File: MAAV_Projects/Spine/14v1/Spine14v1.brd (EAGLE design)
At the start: 124.5 x 101.6 mm, 91 parts, among them J7 MA04-1, Q1 MOSFET-NCHANNELSMD, Q2 MOSFET-NCHANNELSMD, Q21 P-MOSFET-SO8POWER-PAK, Q22 P-MOSFET-SO8POWER-PAK, Q23 P-MOSFET-SO8POWER-PAK, Q24 P-MOSFET-SO8POWER-PAK, Q3 MOSFET-NCHANNELSMD, Q4 MOSFET-NCHANNELSMD, Q5 P-MOSFET-SO8POWER-PAK, Q6 MOSFET-NCHANNELSMD, Q7 MOSFET-NCHANNELSMD, Q8 MOSFET-NCHANNELSMD, U1 ATMEGA328-AU, U3 XC6210

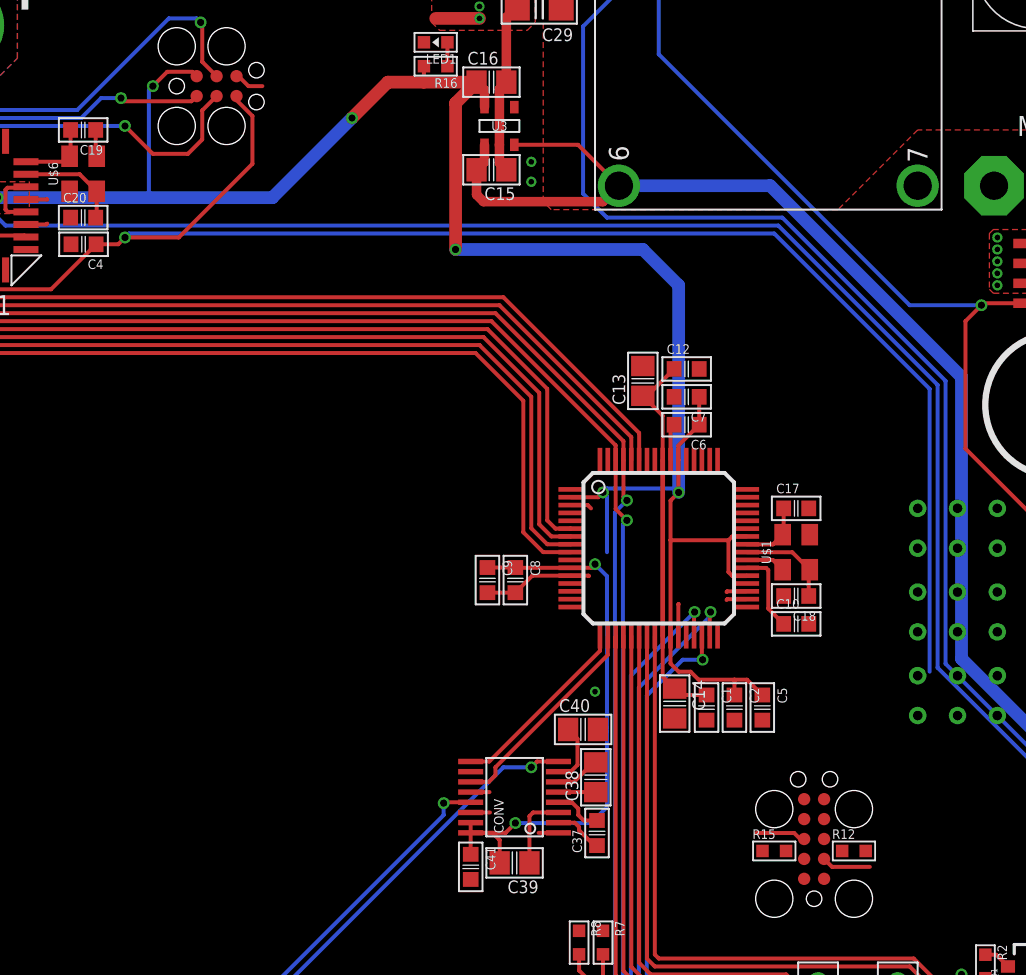
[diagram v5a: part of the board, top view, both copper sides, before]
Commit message: finished JTAG routing. still need to finish the toggle switches
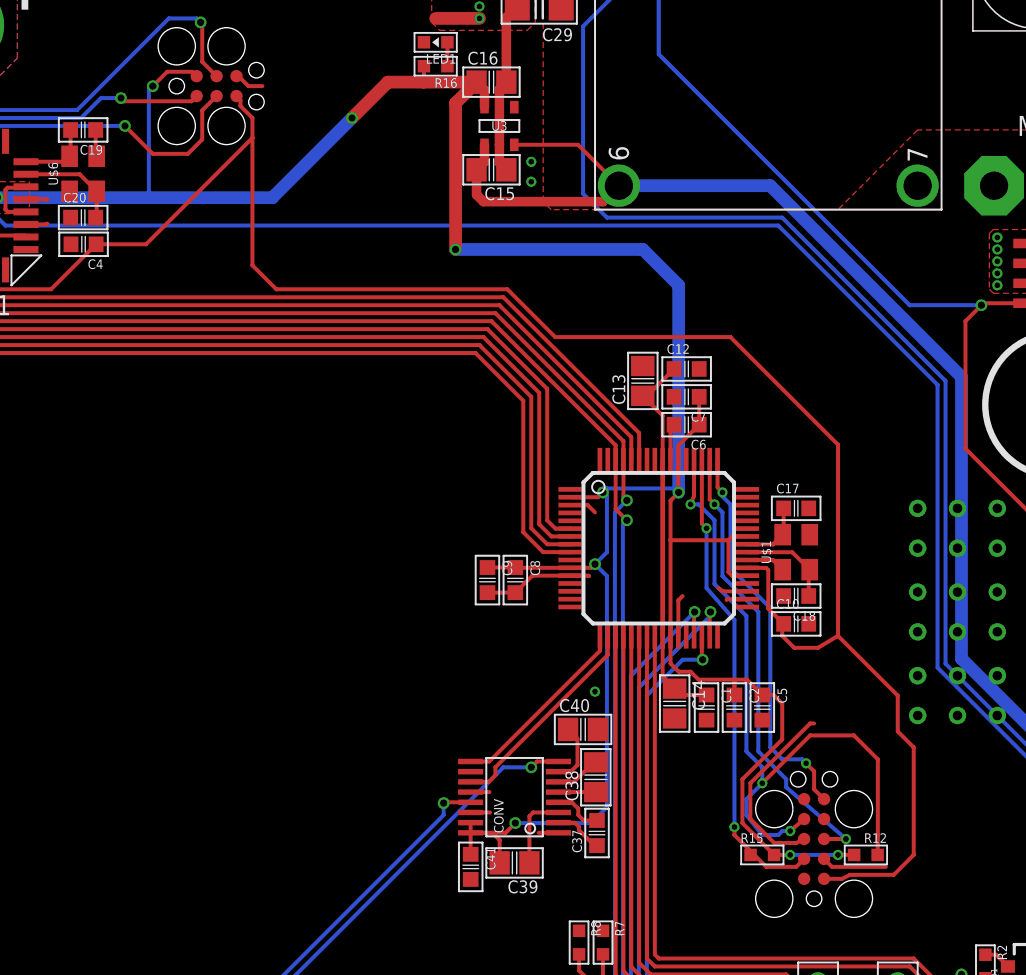
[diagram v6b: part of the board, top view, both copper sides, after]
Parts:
- moved R12 0.80 mm to (84.3, 22.1), turned to 180 degrees
- moved R15 0.80 mm to (77.7, 22.1)
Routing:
- net ICDI_TCK: track 0.00 -> 45.3 mm, vias 0 -> 3
- net ICDI_TMS: track 0.00 -> 30.3 mm, vias 0 -> 2
- net ICDI_TDI: track 0.00 -> 29.3 mm, vias 0 -> 2
- net ICDI_TDO: track 0.00 -> 25.2 mm, vias 0 -> 2
- net +3V3: track 198.7 -> 218.0 mm, vias 10 -> 12
- net RESET: track 143.9 -> 158.9 mm, vias 1 -> 0
- net GND: track 51.1 -> 62.5 mm

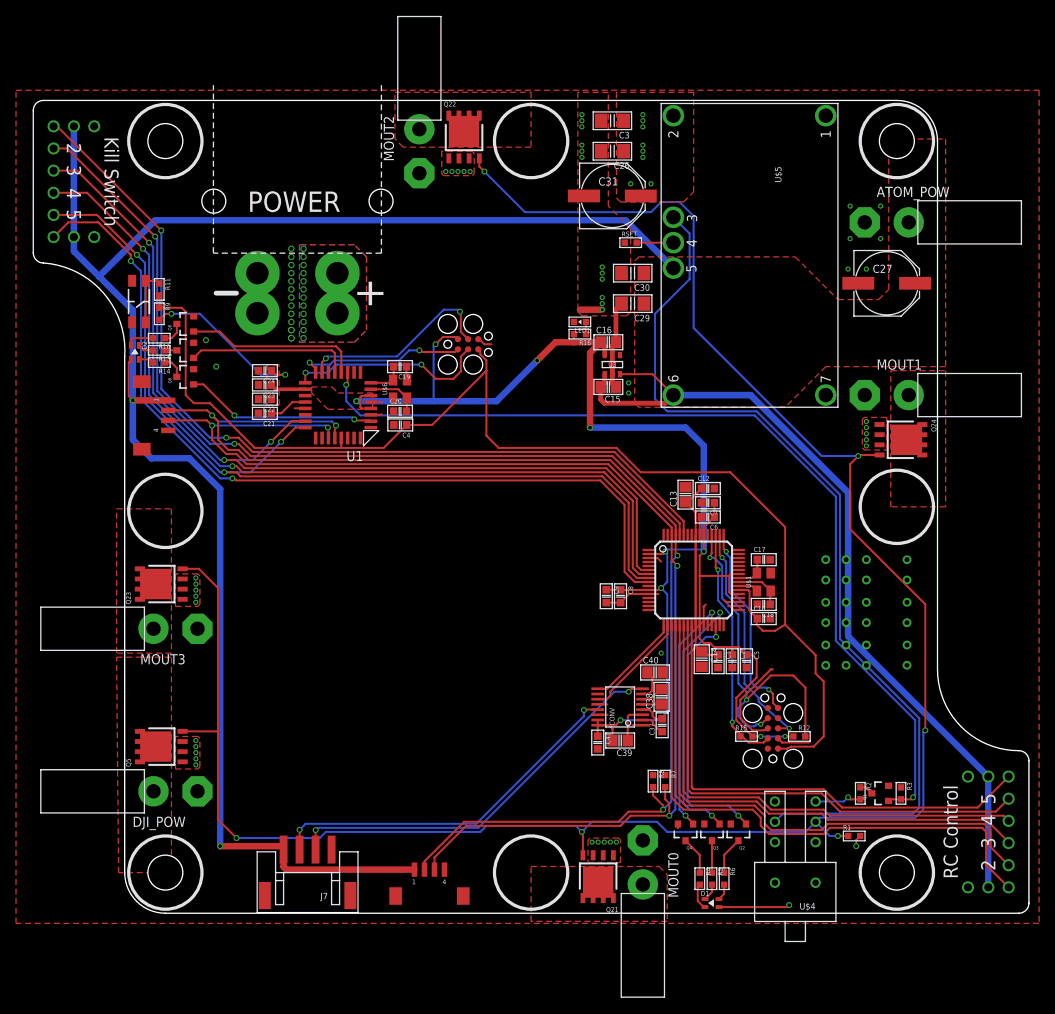
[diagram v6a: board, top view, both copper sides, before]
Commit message: put in toggle switches and finished routing the baord.  Added logo and credits
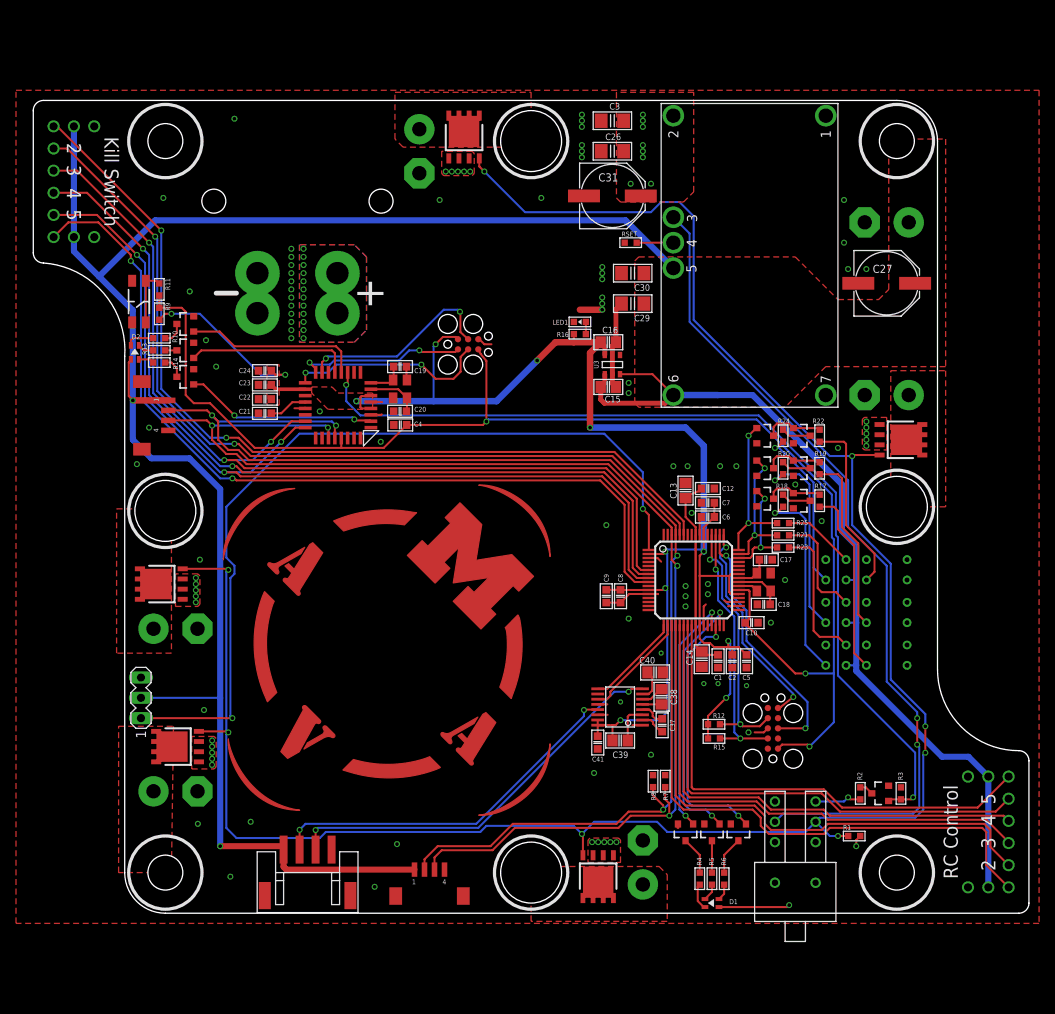
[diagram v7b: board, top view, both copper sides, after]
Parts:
- removed S4: SWITCH_SPDT_ILUMINATED_2COLOR_VERT_ILLUMINATED, Jon_LIB:NKK_VERT_SWITCH_6PIN
- added DJI_SIG: (no value), Jon_LIB:MA03-1
- added Q10, Q11, Q12, Q13, Q14, Q9: MOSFET-NCHANNELSMD, Jon_LIB:SOT23-3
- added R17, R18, R19, R20, R22, R24: 100, Jon_LIB:R0603
- added R21, R23, R25: 1k, Jon_LIB:R0603
- added S_R: (no value), Jon_LIB:TACT-MOM-SMD
- added U$8: (no value), maav-logos:MAAVLOGO_50MM_MASK_ONLY
- S1: value SWITCH_DPDT_VERT_TOGGLE -> SWITCH_SPDT_ILUMINATED_2COLOR_VERT_ILLUMINATED
- S2: value (none) -> SWITCH_SPDT_ILUMINATED_2COLOR_VERT_ILLUMINATED; device Jon_LIB:TACT-MOM-SMD -> Jon_LIB:NKK_VERT_SWITCH_6PIN
- moved S2 98.9 mm to (92.7, 37.6), turned to 90 degrees
- moved R12 10.8 mm to (73.7, 23.6)
- moved S1 10.7 mm to (92.7, 32.3)
- moved S3 5.33 mm to (92.7, 42.9)
- moved R15 4.07 mm to (73.7, 21.8), turned to 180 degrees
- moved Q5 2.03 mm to (6.60, 20.8)
- moved C10 1.61 mm to (78.4, 36.3)
- moved C13 0.51 mm to (70.1, 52.8)
- moved C17 0.25 mm to (80.1, 44.2)
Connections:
- new net DJI_PPM: DJI_SIG.1, U$3.P$1
- new net N$26: Q9.3, R18.1
- new net N$27: Q11.1, Q12.3, R19.1
- new net N$28: Q11.3, R20.1
- new net N$29: R19.2, S2.P$6
- new net N$30: R20.2, S2.P$4
- new net N$31: R23.2, S1.P$2
- new net N$33: R21.2, S2.P$2
- new net N$34: R17.2, S1.P$6
- new net N$37: R18.2, S1.P$4
- new net N$39: Q13.1, Q14.3, R22.1
- new net N$40: Q13.3, R24.1
- new net N$41: R22.2, S3.P$6
- new net N$42: R24.2, S3.P$4
- new net N$43: R25.2, S3.P$2
- new net N$9: Q10.3, Q9.1, R17.1
- new net OPT_SWITCH_1: Q10.1, R23.1, U$3.P$46
- new net OPT_SWITCH_2: Q12.1, R21.1, U$3.P$47
- new net OPT_SWITCH_3: Q14.1, R25.1, U$3.P$48
- net +5V: now also DJI_SIG.2, S1.P$5, S2.P$5, S3.P$5
- net GND: now also DJI_SIG.3, Q10.2, Q11.2, Q12.2, Q13.2, Q14.2, Q9.2, S1.P$1, S2.P$1, S3.P$1, S_R.S, S_R.S1; no longer S2.S, S2.S1
- net N$10: now also S_R.P, S_R.P1; no longer S2.P, S2.P1
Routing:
- net DJI_PPM: track 0.00 -> 106.5 mm, vias 0 -> 2
- net N$37: track 0.00 -> 24.8 mm, vias 0 -> 1
- net N$30: track 0.00 -> 24.6 mm, vias 0 -> 1
- net N$34: track 0.00 -> 23.3 mm
- net N$41: track 0.00 -> 22.3 mm
- net N$29: track 0.00 -> 22.3 mm
- net N$42: track 0.00 -> 20.8 mm, vias 0 -> 1
- net OPT_SWITCH_3: track 0.00 -> 19.8 mm, vias 0 -> 2
- net N$31: track 0.00 -> 18.0 mm
- net OPT_SWITCH_2: track 0.00 -> 17.0 mm, vias 0 -> 2
- net +5V: track 353.6 -> 369.4 mm
- net GND: track 62.5 -> 48.2 mm, vias 37 -> 73
- net N$33: track 0.00 -> 13.9 mm
- net OPT_SWITCH_1: track 0.00 -> 13.5 mm, vias 0 -> 2
- net ICDI_TCK: track 45.3 -> 32.2 mm, vias 3 -> 2
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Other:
- board text added: "Andrew Wagenmaker"
- board text added: "Design By:"
- board text added: "Ian Lin"
- board text added: "Jason Leung"
- board text added: "John Connolly"
- board text added: "Jonathan Kurzer"
- board text added: "July 2014"
- board text added: "MAAV Spine Rev 14v1"
- board text added: "Matthew Sauve"
- board text added: "Michigan Autonomous Aerial Vehicles"
- board text added: "Selection switches for the Tiva"
- board text added: "University of Michigan"
- board text removed: "Perhaps some switches to the Tiva"

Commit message: Spine 14v1 boards sent to print house
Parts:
- added U$7: (no value), BlockM:BLOCK-M-DOUBLE-STACKED-10MM-MASK
- added U$9: (no value), BlockM:BLOCK-M-DOUBLE-STACKED-10MM
- moved LED1 0.25 mm to (56.9, 74.2)
- moved R16 0.25 mm to (56.9, 72.6)
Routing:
- net N$38: track 0.00 -> 1.09 mm
- net ICDI_TMS: track 32.7 -> 33.4 mm
- net +3V3: track 213.9 -> 214.6 mm
- net GND: vias 73 -> 77
- added copper zone on layer 16, net GND
